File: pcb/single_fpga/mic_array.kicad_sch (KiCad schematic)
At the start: 15 parts, among them U110 CDCLVC1112PW, Y1 ECS-TXO-5032

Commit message: Fixed power and gnd. ERC-clean.
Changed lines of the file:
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@@
 	)
 	(global_label "+3V3_ETH"
-		(shape input)
+		(shape passive)
 		(at 226.06 132.08 180)
 		(fields_autoplaced yes)
@@
 		)
 		(property "Intersheetrefs" "${INTERSHEET_REFS}"
-			(at 213.5801 132.08 0)
+			(at 214.6914 132.08 0)
 			(hide yes)
 			(show_name no)
@@
 	)
 	(global_label "+3V3_ETH"
-		(shape input)
+		(shape passive)
 		(at 135.89 140.97 0)
 		(fields_autoplaced yes)
@@
 		)
 		(property "Intersheetrefs" "${INTERSHEET_REFS}"
-			(at 148.3699 140.97 0)
+			(at 147.2586 140.97 0)
 			(hide yes)
 			(show_name no)
@@
 	)
 	(global_label "+3V6"
-		(shape input)
+		(shape passive)
 		(at 227.33 57.15 180)
 		(fields_autoplaced yes)
@@
 		)
 		(property "Intersheetrefs" "${INTERSHEET_REFS}"
-			(at 219.2648 57.15 0)
+			(at 220.3761 57.15 0)
 			(hide yes)
 			(show_name no)
@@
 	)
 	(global_label "+3V6"
-		(shape input)
+		(shape passive)
 		(at 228.6 95.25 180)
 		(fields_autoplaced yes)
@@
 		)
 		(property "Intersheetrefs" "${INTERSHEET_REFS}"
-			(at 220.5348 95.25 0)
+			(at 221.6461 95.25 0)
 			(hide yes)
 			(show_name no)
@@
 	)
 	(global_label "+3V3_ETH"
-		(shape input)
+		(shape passive)
 		(at 44.45 139.7 180)
 		(fields_autoplaced yes)
@@
 		)
 		(property "Intersheetrefs" "${INTERSHEET_REFS}"
-			(at 31.9701 139.7 0)
-			(hide yes)
-			(show_name no)
+			(at 33.0814 139.7 0)
+			(hide yes)
+			(show_name no)

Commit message: Fixed power rails. Fixed C3. Changed U4. ERC FEB.
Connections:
- net +3V3_ETH renamed CLK_3V3
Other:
- moved on the sheet: C101, C97, C99, VR2

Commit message: Added TXCO divide by FPGA.
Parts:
- added R15: 33, PCM_SparkFun-Resistor:R_0603_1608Metric, symbol PCM_SparkFun-Resistor:10k_0603
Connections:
- net TCXO_CLK: now also R15.1; no longer U110.1 (CLKIN), Y1.3 (OUTPUT)
- new net: R15.2, Y1.3 (OUTPUT)
- new net PDM_CLK: U110.1 (CLKIN)
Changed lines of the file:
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@@
 	(wire
 		(pts
+			(xy 236.22 158.75) (xy 233.68 158.75)
+		)
+		(stroke
+			(width 0)
+			(type default)
+		)
+	)
+	(wire
+		(pts
 			(xy 232.41 80.01) (xy 232.41 78.74)
 		)
@@
 	(wire
 		(pts
-			(xy 245.11 158.75) (xy 233.68 158.75)
-		)
-		(stroke
-			(width 0)
-			(type default)
-		)
-	)
-	(wire
-		(pts
 			(xy 123.19 176.53) (xy 130.81 176.53)
 		)
@@
 	(wire
 		(pts
+			(xy 245.11 158.75) (xy 241.3 158.75)
+		)
+		(stroke
+			(width 0)
+			(type default)
+		)
+	)
+	(wire
+		(pts
 			(xy 59.69 156.21) (xy 59.69 148.59)
 		)
@@
 		)
 	)
-	(global_label "TCXO_CLK"
+	(global_label "PDM_CLK"
 		(shape input)
 		(at 44.45 153.67 180)
@@
 	)
 	(symbol
+		(lib_id "PCM_SparkFun-Resistor:10k_0603")
+		(at 238.76 158.75 0)
+		(unit 1)
+		(body_style 1)
+		(exclude_from_sim no)
+		(in_bom yes)
+		(on_board yes)
+		(in_pos_files yes)
+		(dnp no)
+		(property "Reference" "R15"
+			(at 238.506 161.036 0)
+			(show_name no)
+			(do_not_autoplace no)
+			(effects
+				(font
+					(size 1.27 1.27)
+				)
+			)
+		)
+		(property "Value" "33"
+			(at 238.506 162.814 0)
+			(show_name no)
+			(do_not_autoplace no)
+			(effects
+				(font
+					(size 1.27 1.27)
+				)
+			)
+		)
+		(property "Footprint" "PCM_SparkFun-Resistor:R_0603_1608Metric"
+			(at 238.76 158.75 0)
+			(hide yes)
+			(show_name no)
+			(do_not_autoplace no)
+			(effects
+				(font
+					(size 1.27 1.27)
+				)
+			)
+		)
+		(property "Datasheet" "https://www.vishay.com/docs/20035/dcrcwe3.pdf"
+			(at 238.76 158.75 0)
+			(hide yes)
+			(show_name no)
+			(do_not_autoplace no)
+			(effects
+				(font
+					(size 1.27 1.27)
+				)
+			)
+		)
+		(property "Description" "Resistor"
+			(at 238.76 158.75 0)
+			(hide yes)
+			(show_name no)
+			(do_not_autoplace no)
+			(effects
+				(font
+					(size 1.27 1.27)
+				)
+			)
+		)
+		(property "PROD_ID" ""
+			(at 238.76 158.75 0)
+			(hide yes)
+			(show_name no)
+			(do_not_autoplace no)
+			(effects
+				(font
+					(size 1.27 1.27)
+				)
+			)
+		)
+		(pin "1"
+		)
+		(pin "2"
+		)
+		(instances
+			(project "mic_array"
+				(path "/12638caa-1907-413e-8e98-06abbbf6ccbc"
+					(reference "R15")
+					(unit 1)
+				)
+			)
+		)
+	)
+	(symbol
 		(lib_id "power:GND")
 		(at 251.46 80.01 0)
@@
 			"0c43ee04-cf33-4ec3-bc90-01842c8c47bc" "11e1f8a7-ccbe-4f93-bf34-baac9ccea104"
 			"1441a65f-9e0a-4fbb-9aea-91c889fb87a2" "2dcf9488-30b2-46b5-a3ec-ca4687c223e3"
-			"58925e13-98d6-4727-a72d-7bd5fa21d73c" "70eb1d76-8c7c-49cc-8a23-af30f51e9e5e"
-			"8e39dec4-fa64-4bba-9b80-4e4136f1cc73" "8f39ad8a-ff66-4761-9ffd-615b8819a5d3"
-			"d14e62a1-58d3-4051-bd6e-e48ef22b8999" "d1973912-4cfb-491e-a741-fa687ac05d13"
-			"d5799d01-5e4b-4364-9530-a008c6d06132" "dcc917c2-c356-4014-b24e-954f046c8e7b"
-			"f8c53211-524a-4a72-9661-10537c9aa3c7"
+			"58925e13-98d6-4727-a72d-7bd5fa21d73c" "8e39dec4-fa64-4bba-9b80-4e4136f1cc73"
+			"8f39ad8a-ff66-4761-9ffd-615b8819a5d3" "d14e62a1-58d3-4051-bd6e-e48ef22b8999"
+			"d1973912-4cfb-491e-a741-fa687ac05d13" "d5799d01-5e4b-4364-9530-a008c6d06132"
+			"dcc917c2-c356-4014-b24e-954f046c8e7b" "f8c53211-524a-4a72-9661-10537c9aa3c7"
 		)
 	)

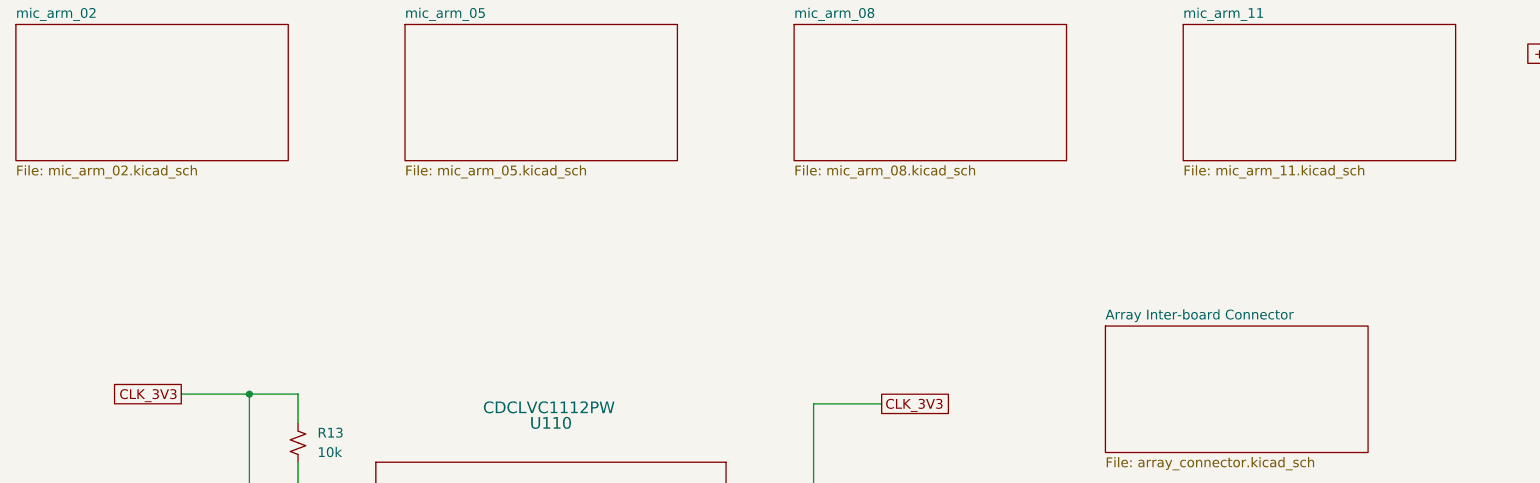
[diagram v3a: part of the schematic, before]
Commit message: Added stitching caps to worst clock lines.
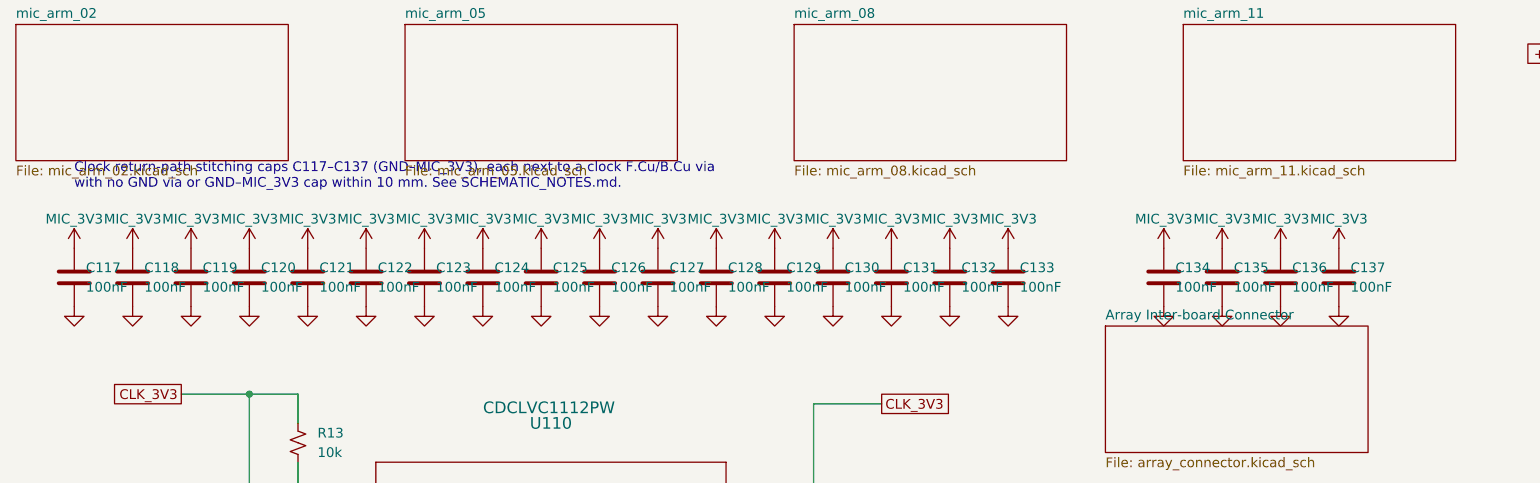
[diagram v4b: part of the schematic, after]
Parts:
- added C117, C118, C119, C120, C121, C122, C123, C124, C125, C126, C127, C128, C129, C130, C131, C132, C133, C134, C135, C136, C137: 100nF, Capacitor_SMD:C_0603_1608Metric, symbol Device:C
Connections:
- net GND: now also C117.2, C118.2, C119.2, C120.2, C121.2, C122.2, C123.2, C124.2, C125.2, C126.2, C127.2, C128.2, C129.2, C130.2, C131.2, C132.2, C133.2, C134.2, C135.2, C136.2, C137.2
- net MIC_3V3: now also C117.1, C118.1, C119.1, C120.1, C121.1, C122.1, C123.1, C124.1, C125.1, C126.1, C127.1, C128.1, C129.1, C130.1, C131.1, C132.1, C133.1, C134.1, C135.1, C136.1, C137.1
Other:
- note added: "Clock return-path stitching caps C117–C137 (GND–MIC_3V3), each next to a clock F.Cu/B.Cu via with no GND via or GND–MIC_3V3 cap within 10 mm. See SCHEMATIC_NOTES.md."

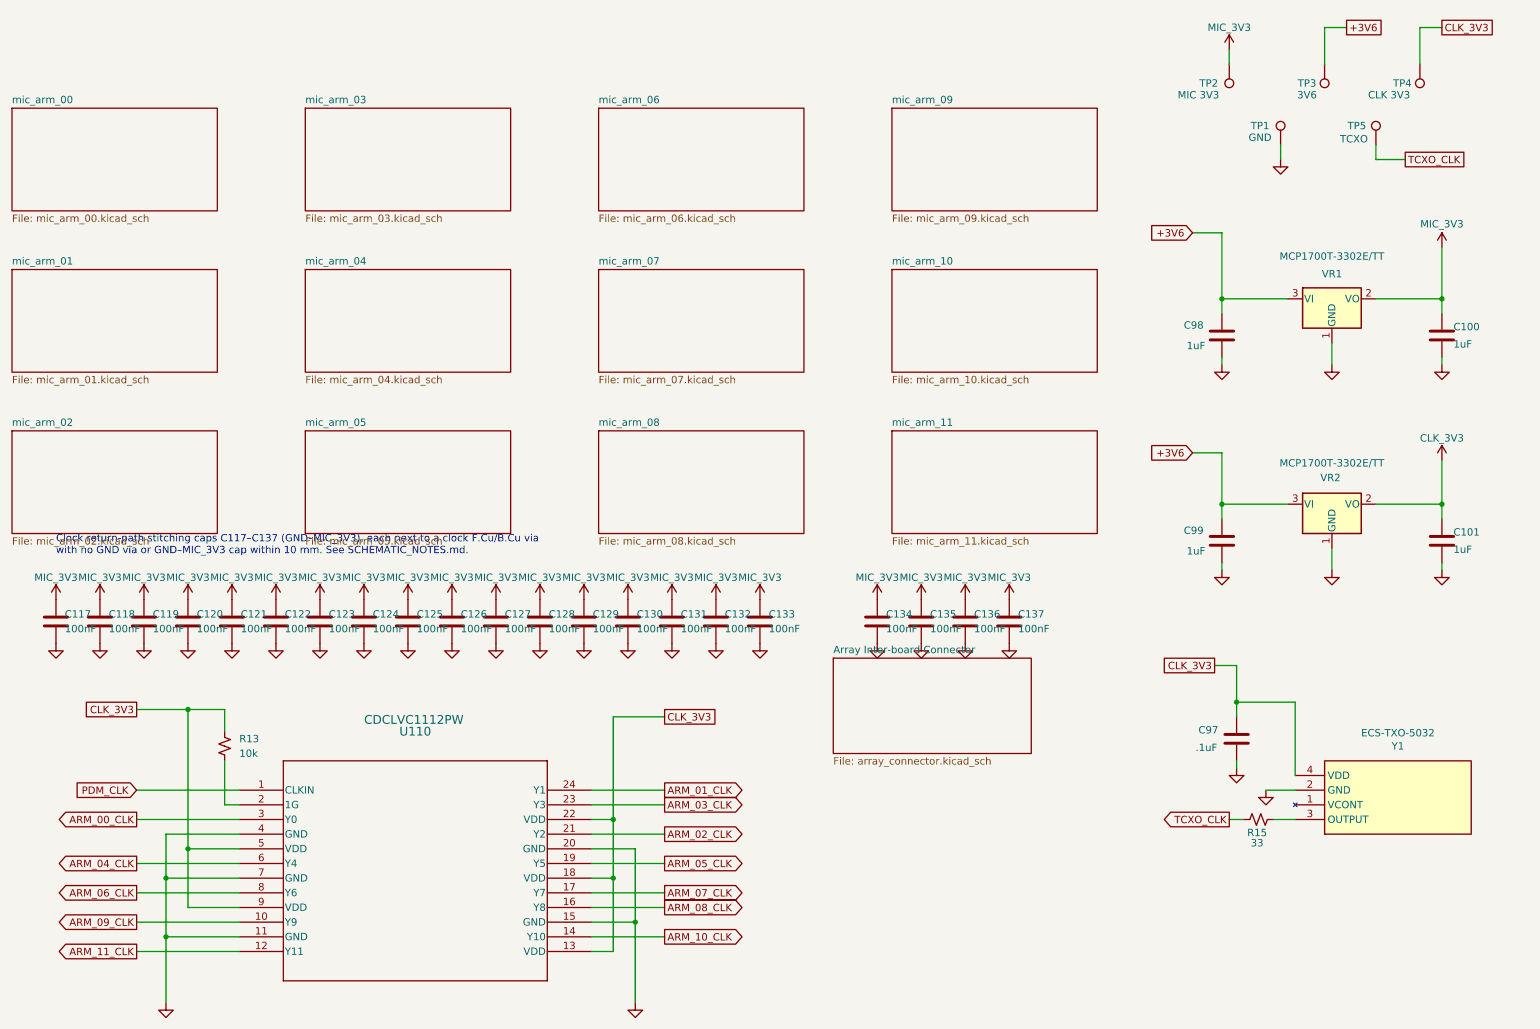
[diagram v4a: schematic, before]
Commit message: Added stitching caps.
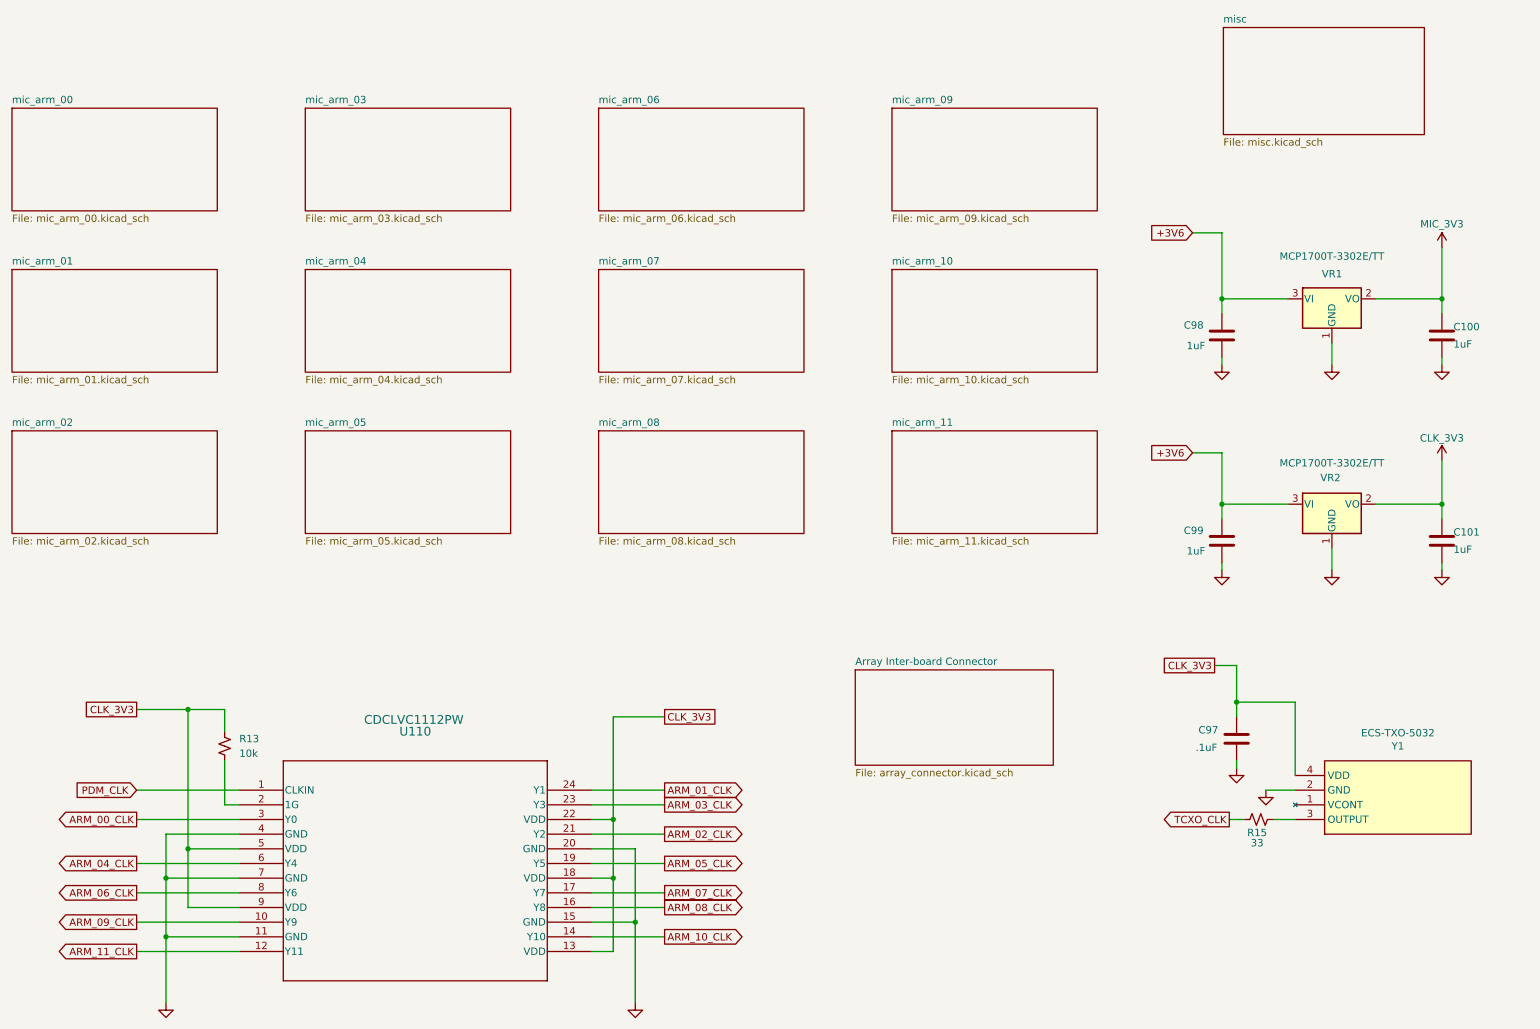
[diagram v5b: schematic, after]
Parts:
- removed C117, C118, C119, C120, C121, C122, C123, C124, C125, C126, C127, C128, C129, C130, C131, C132, C133, C134, C135, C136, C137: 100nF, Capacitor_SMD:C_0603_1608Metric, symbol Device:C
- removed TP1: GND, TestPoint:TestPoint_THTPad_D2.0mm_Drill1.0mm, symbol Connector:TestPoint
- removed TP2: MIC 3V3, TestPoint:TestPoint_THTPad_D2.0mm_Drill1.0mm, symbol Connector:TestPoint
- removed TP3: 3V6, TestPoint:TestPoint_THTPad_D2.0mm_Drill1.0mm, symbol Connector:TestPoint
- removed TP4: CLK 3V3, TestPoint:TestPoint_THTPad_D2.0mm_Drill1.0mm, symbol Connector:TestPoint
- removed TP5: TCXO, TestPoint:TestPoint_THTPad_D2.0mm_Drill1.0mm, symbol Connector:TestPoint
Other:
- added sheet misc (misc.kicad_sch)
- note removed: "Clock return-path stitching caps C117–C137 (GND–MIC_3V3), each next to a clock F.Cu/B.Cu via with no GND via or GND–MIC_3V3 cap within 10 mm. See SCHEMATIC_NOTES.md."

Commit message: Renamed.
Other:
- sheet misc renamed mic_array_misc
- sheet mic_array_misc: file misc.kicad_sch -> mic_array_misc.kicad_sch
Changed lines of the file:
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@@
 			(color 0 0 0 0)
 		)
-		(property "Sheetname" "misc"
+		(property "Sheetname" "mic_array_misc"
 			(at 232.664 20.8784 0)
 			(show_name no)
@@
 			)
 		)
-		(property "Sheetfile" "misc.kicad_sch"
+		(property "Sheetfile" "mic_array_misc.kicad_sch"
 			(at 232.664 40.7166 0)
 			(show_name no)
